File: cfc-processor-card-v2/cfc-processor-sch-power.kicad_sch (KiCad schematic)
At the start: 93 parts, among them Q2 PMV45EN, Q3 DMP2240UDM, Q4 PMV45EN, Q5 DMP3050LVT-7, Q6 DMP3050LVT-7, U12 MIC842LYC5, U13 MIC842LYC5, U14 MAX4211FETE, U15 TPS62112, U16 MAX7310ATE+, U5 TS5A21366

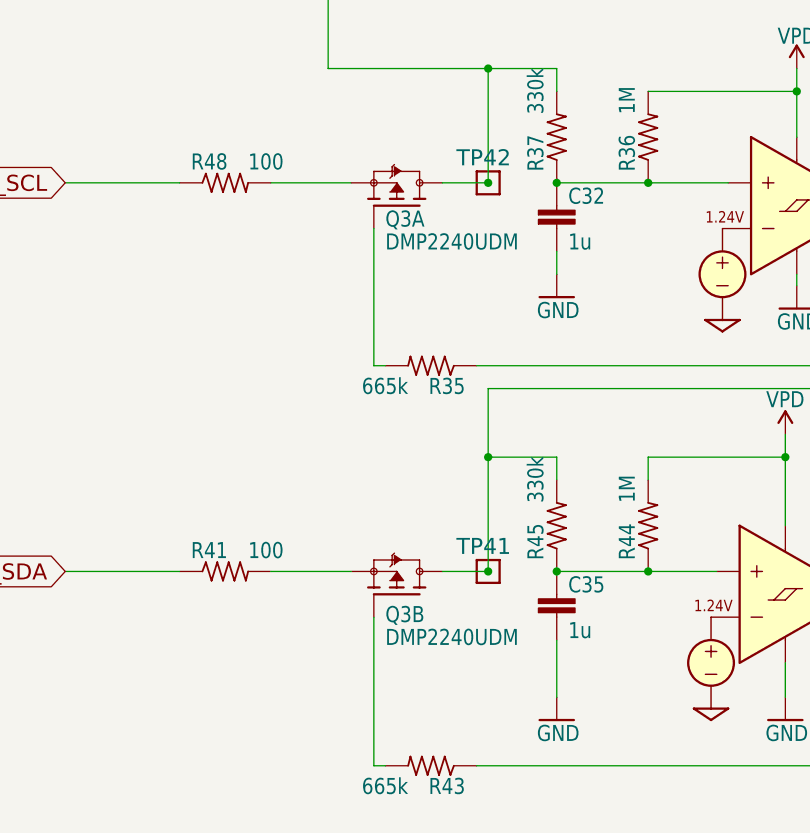
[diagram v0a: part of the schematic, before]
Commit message: Fixed up crappy symbol on OPD; no change to layout, just schematic and link to PCB.
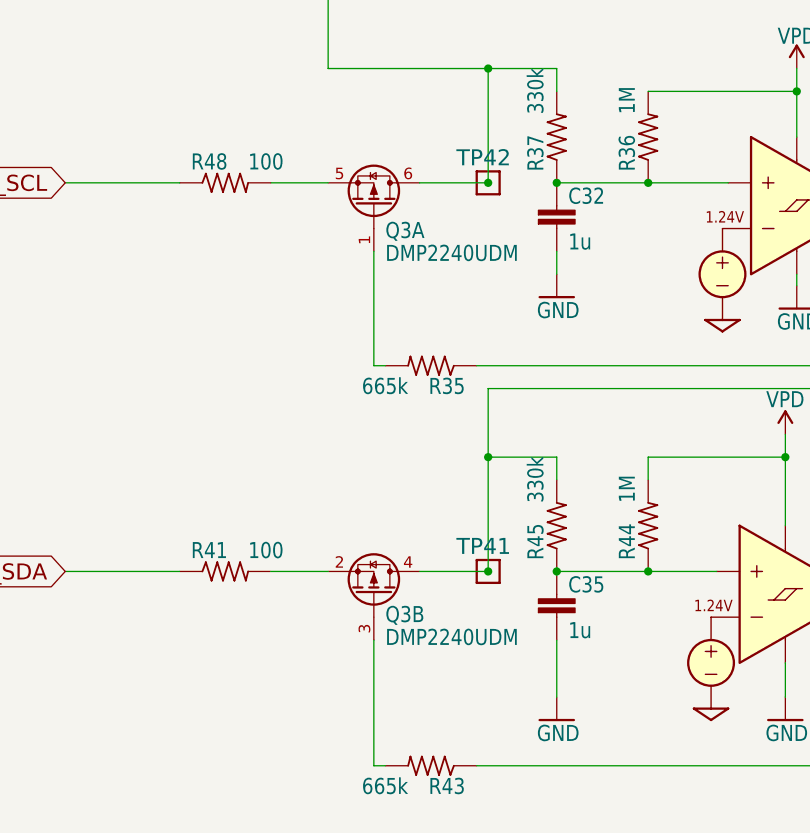
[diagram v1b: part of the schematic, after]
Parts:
- Q3: symbol cfc-card-eagle-import:Q-MOSFET-PCH-dual-SOT23-6_MOSFET-PCH-SOT23-6 -> Transistor_FET:Q_Dual_PMOS_G1S2G2D2S1D1
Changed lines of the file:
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@@
 	(wire
 		(pts
-			(xy 92.71 245.11) (xy 92.71 228.6)
+			(xy 92.71 245.11) (xy 92.71 231.14)
 		)
 		(stroke
@@
 	(wire
 		(pts
-			(xy 105.41 180.34) (xy 100.33 180.34)
+			(xy 105.41 180.34) (xy 97.79 180.34)
 		)
 		(stroke
@@
 	(wire
 		(pts
-			(xy 90.17 223.52) (xy 81.28 223.52)
+			(xy 87.63 223.52) (xy 81.28 223.52)
 		)
 		(stroke
@@
 	(wire
 		(pts
-			(xy 92.71 200.66) (xy 92.71 185.42)
+			(xy 92.71 200.66) (xy 92.71 187.96)
 		)
 		(stroke
@@
 	(wire
 		(pts
-			(xy 105.41 223.52) (xy 100.33 223.52)
+			(xy 105.41 223.52) (xy 97.79 223.52)
 		)
 		(stroke
@@
 	(wire
 		(pts
-			(xy 90.17 180.34) (xy 81.28 180.34)
+			(xy 87.63 180.34) (xy 81.28 180.34)
 		)
 		(stroke
@@
 	)
 	(symbol
-		(lib_id "cfc-card-eagle-import:Q-MOSFET-PCH-dual-SOT23-6_MOSFET-PCH-SOT23-6")
-		(at 95.25 226.06 90)
+		(lib_id "Transistor_FET:Q_Dual_PMOS_G1S2G2D2S1D1")
+		(at 92.71 226.06 270)
+		(mirror x)
 		(unit 2)
 		(exclude_from_sim no)
@@
 					(size 1.778 1.5113)
 				)
-				(justify right top)
+				(justify left top)
 			)
 		)
@@
 					(size 1.778 1.5113)
 				)
-				(justify right top)
+				(justify left top)
 			)
 		)
 		(property "Footprint" "Package_TO_SOT_SMD:SOT-23-6"
-			(at 95.25 226.06 0)
+			(at 92.71 224.79 0)
 			(effects
 				(font
@@
 			)
 		)
-		(property "Datasheet" "https://www.diodes.com/assets/Datasheets/ds31197.pdf"
-			(at 95.25 226.06 0)
+		(property "Datasheet" "~"
+			(at 92.71 224.79 0)
 			(effects
 				(font
@@
 			)
 		)
-		(property "Description" "Dual Mosfet Array 20V 2A 600mW Surface Mount SOT-26"
-			(at 95.25 226.06 0)
+		(property "Description" "Dual PMOS transistor, 6 pin package"
+			(at 92.71 226.06 0)
 			(effects
 				(font
@@
 		)
 		(property "DIS" "DigiKey"
-			(at 95.25 226.06 90)
+			(at 92.71 226.06 90)
 			(effects
 				(font
@@
 		)
 		(property "DPN" "DMP2240UDMDICT-ND"
-			(at 95.25 226.06 90)
+			(at 92.71 226.06 90)
 			(effects
 				(font
@@
 		)
 		(property "MFR" "Diodes Inc"
-			(at 95.25 226.06 90)
+			(at 92.71 226.06 90)
 			(effects
 				(font
@@
 		)
 		(property "MPN" "DMP2240UDM"
-			(at 95.25 226.06 90)
+			(at 92.71 226.06 90)
 			(effects
 				(font
@@
 			)
 		)
+		(property "Value_1" ""
+			(at 92.71 226.06 0)
+			(effects
+				(font
+					(size 1.778 1.5113)
+				)
+				(justify left bottom)
+				(hide yes)
+			)
+		)
 		(pin "1"
 		)
@@
 	)
 	(symbol
-		(lib_id "cfc-card-eagle-import:Q-MOSFET-PCH-dual-SOT23-6_MOSFET-PCH-SOT23-6")
-		(at 95.25 182.88 90)
+		(lib_id "Transistor_FET:Q_Dual_PMOS_G1S2G2D2S1D1")
+		(at 92.71 182.88 270)
+		(mirror x)
 		(unit 1)
 		(exclude_from_sim no)
@@
 		(dnp no)
 		(property "Reference" "Q3"
-			(at 93.98 185.42 90)
+			(at 93.98 186.69 90)
 			(effects
 				(font
 					(size 1.778 1.5113)
 				)
-				(justify right top)
+				(justify left top)
 			)
 		)
 		(property "Value" "DMP2240UDM"
-			(at 93.98 187.96 90)
+			(at 93.98 189.23 90)
 			(effects
 				(font
 					(size 1.778 1.5113)
 				)
-				(justify right top)
+				(justify left top)
 			)
 		)
 		(property "Footprint" "Package_TO_SOT_SMD:SOT-23-6"
-			(at 95.25 182.88 0)
+			(at 92.71 181.61 0)
 			(effects
 				(font
@@
 			)
 		)
-		(property "Datasheet" "https://www.diodes.com/assets/Datasheets/ds31197.pdf"
-			(at 95.25 182.88 0)
+		(property "Datasheet" "~"
+			(at 92.71 181.61 0)
 			(effects
 				(font
@@
 			)
 		)
-		(property "Description" "Dual Mosfet Array 20V 2A 600mW Surface Mount SOT-26"
-			(at 95.25 182.88 0)
+		(property "Description" "Dual PMOS transistor, 6 pin package"
+			(at 92.71 182.88 0)
 			(effects
 				(font
@@
 		)
 		(property "DIS" "DigiKey"
-			(at 95.25 182.88 90)
+			(at 92.71 182.88 90)
 			(effects
 				(font
@@
 		)
 		(property "DPN" "DMP2240UDMDICT-ND"
-			(at 95.25 182.88 90)
+			(at 92.71 182.88 90)
 			(effects
 				(font
@@
 		)
 		(property "MFR" "Diodes Inc"
-			(at 95.25 182.88 90)
+			(at 92.71 182.88 90)
 			(effects
 				(font
@@
 		)
 		(property "MPN" "DMP2240UDM"
-			(at 95.25 182.88 90)
+			(at 92.71 182.88 90)
 			(effects
 				(font
@@
 				(hide yes)
 			)
+		)
+		(property "Value_1" ""
+			(at 92.71 182.88 0)
+			(effects
+				(font
+					(size 1.778 1.5113)
+				)
+				(justify left bottom)
+				(hide yes)
+			)

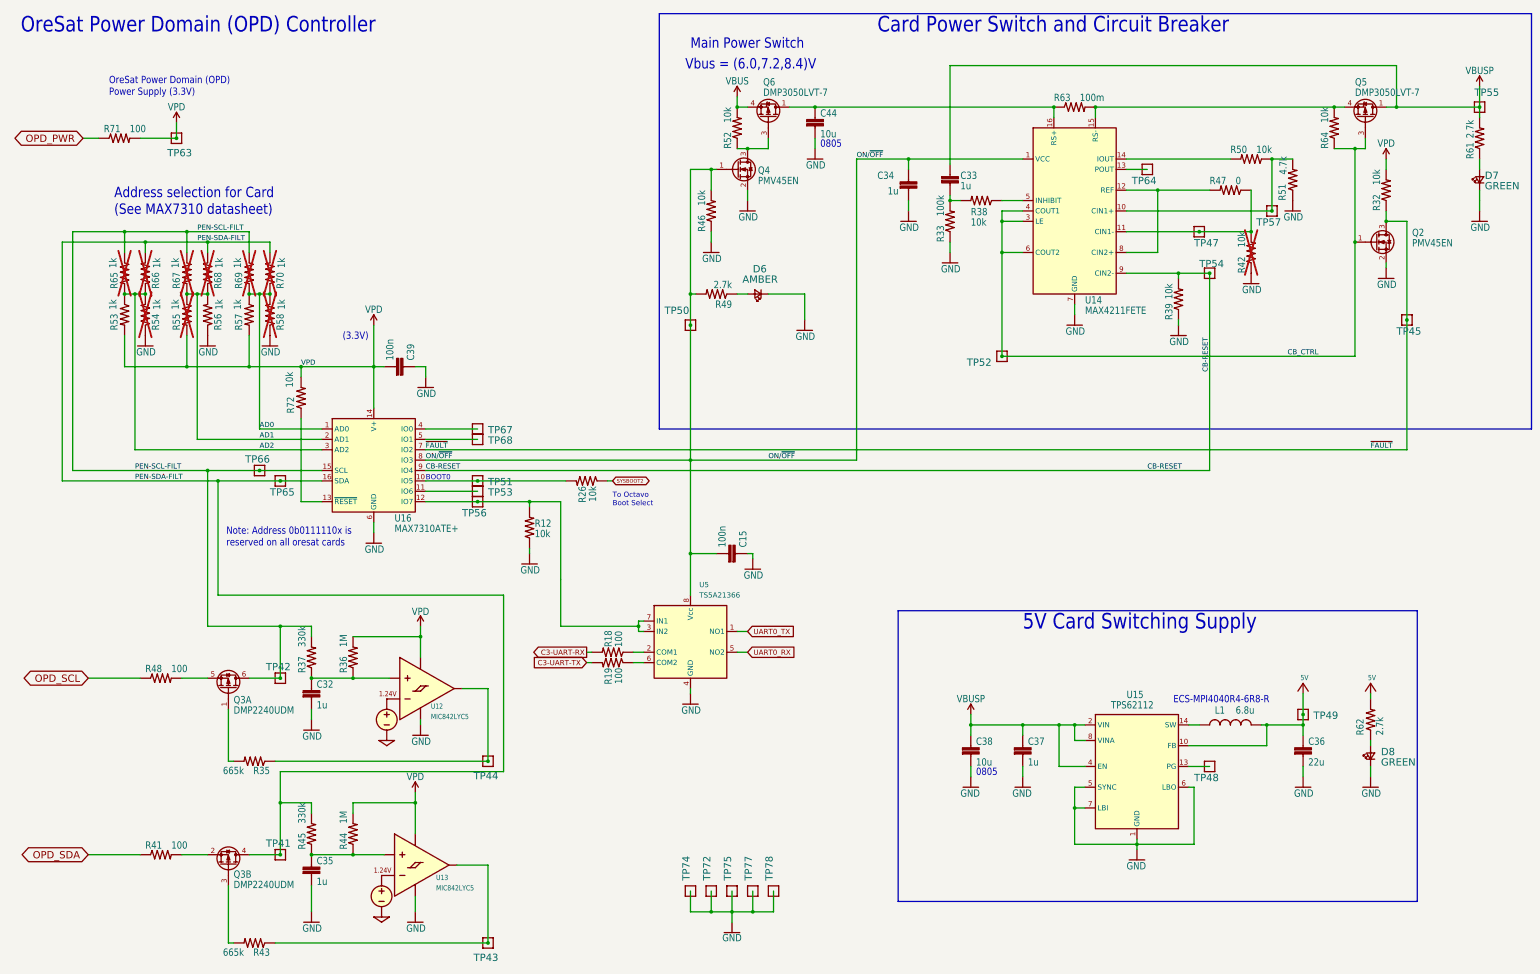
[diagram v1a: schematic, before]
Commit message: CFC processor schematic Change
changed to hierarchy view, changed all global net labels to hierarchy labels, changed all resistor, capacitor, and ground symbols to modern oresat labels. Deleted connectors sheet and added .history to gitignore.
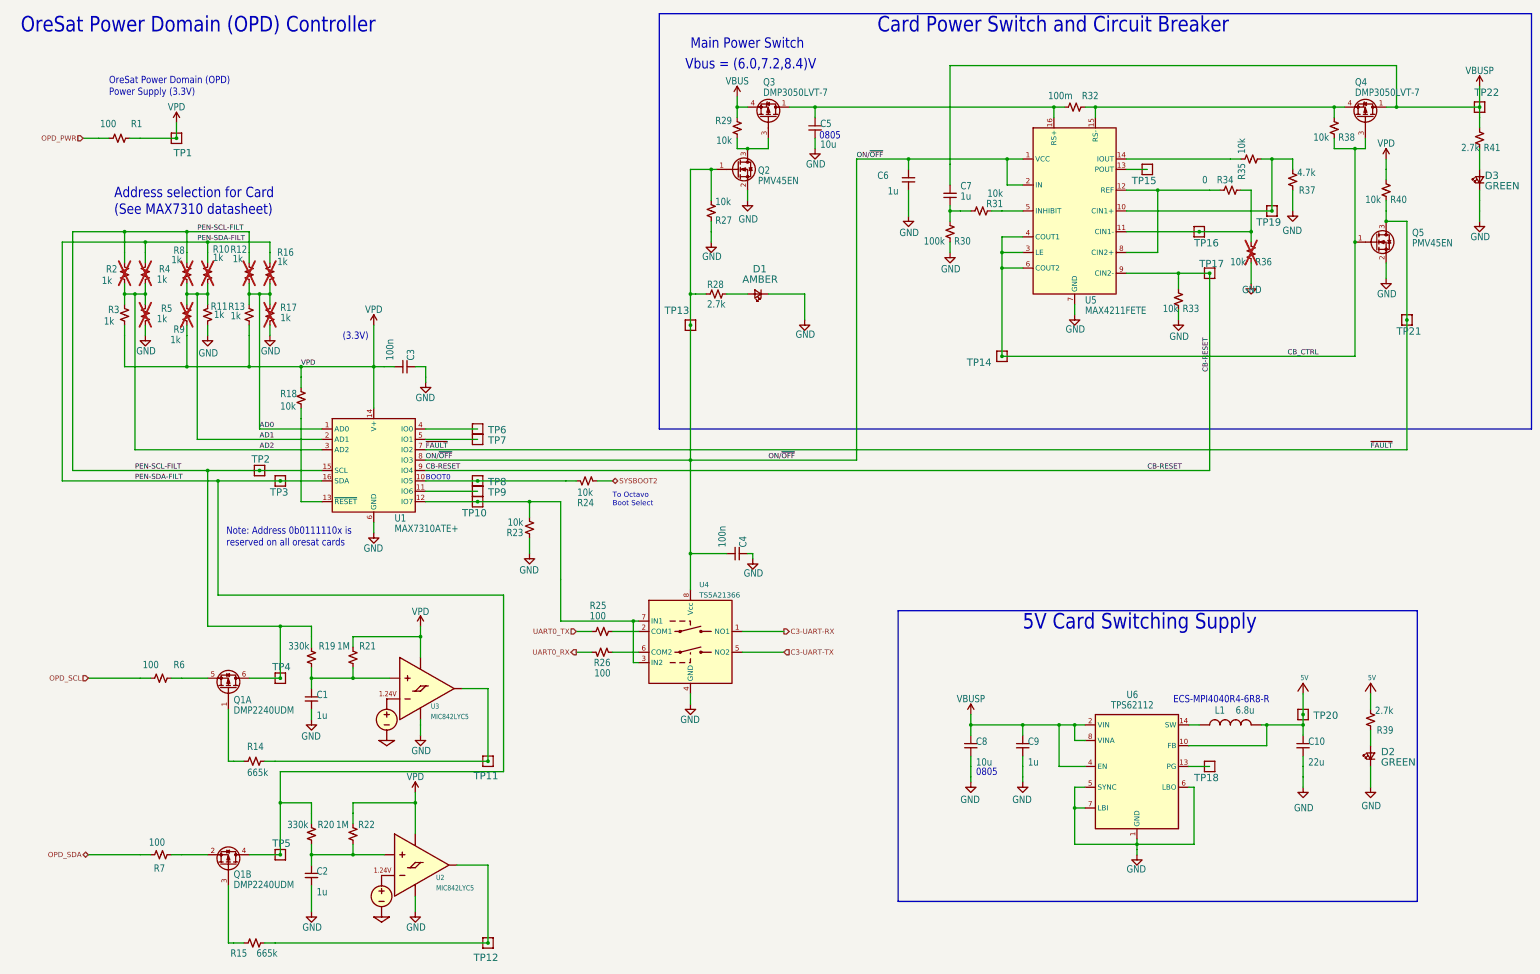
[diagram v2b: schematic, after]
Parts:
- removed TP72, TP74, TP75, TP77, TP78: TEST-POINT, cfc-card:2MM-TEST-POINT, symbol cfc-card-eagle-import:TEST-POINT
- C1: renamed from C32; symbol cfc-card-eagle-import:C-EU0805-B-NOSILK -> Device:C_Small
- C10: renamed from C36; symbol cfc-card-eagle-import:C-EUC1210 -> Device:C_Small
- C2: renamed from C35; symbol cfc-card-eagle-import:C-EU0805-B-NOSILK -> Device:C_Small
- C3: renamed from C39; symbol cfc-card-eagle-import:C-EU0603-A -> Device:C_Small
- C4: renamed from C15; symbol cfc-card-eagle-import:C-EU0603-A -> Device:C_Small
- C5: renamed from C44; symbol cfc-card-eagle-import:C-EU0805-B -> Device:C_Small
- C6: renamed from C34; symbol cfc-card-eagle-import:C-EU0603-A -> Device:C_Small
- C7: renamed from C33; symbol cfc-card-eagle-import:C-EU0603-A -> Device:C_Small
- C8: renamed from C38; symbol cfc-card-eagle-import:C-EU0805-B -> Device:C_Small
- C9: renamed from C37; symbol cfc-card-eagle-import:C-EU0603-A -> Device:C_Small
- R1: renamed from R71; symbol cfc-card-eagle-import:R-US_0603-A -> Device:R_Small_US
- R10: renamed from R68; symbol cfc-card-eagle-import:R-US_0603-A -> Device:R_Small_US
- R11: renamed from R56; symbol cfc-card-eagle-import:R-US_0603-A -> Device:R_Small_US
- R12: renamed from R69; symbol cfc-card-eagle-import:R-US_0603-A -> Device:R_Small_US
- R13: renamed from R57; symbol cfc-card-eagle-import:R-US_0603-A -> Device:R_Small_US
- R14: renamed from R35; symbol cfc-card-eagle-import:R-US_0603-A -> Device:R_Small_US
- R15: renamed from R43; symbol cfc-card-eagle-import:R-US_0603-A -> Device:R_Small_US
- R16: renamed from R70; symbol cfc-card-eagle-import:R-US_0603-A -> Device:R_Small_US
- R17: renamed from R58; symbol cfc-card-eagle-import:R-US_0603-A -> Device:R_Small_US
- R18: renamed from R72; symbol cfc-card-eagle-import:R-US_0603-A -> Device:R_Small_US
- R19: renamed from R37; symbol cfc-card-eagle-import:R-US_0603-A -> Device:R_Small_US
- R2: renamed from R65; symbol cfc-card-eagle-import:R-US_0603-A -> Device:R_Small_US
- R20: renamed from R45; symbol cfc-card-eagle-import:R-US_0603-A -> Device:R_Small_US
- R21: renamed from R36; symbol cfc-card-eagle-import:R-US_0603-A -> Device:R_Small_US
- R22: renamed from R44; symbol cfc-card-eagle-import:R-US_0603-A -> Device:R_Small_US
- R23: renamed from R12; symbol cfc-card-eagle-import:R-US_0603-A -> Device:R_Small_US
- R24: renamed from R26; symbol cfc-card-eagle-import:R-US_0603-A -> Device:R_Small_US
- R25: renamed from R18; symbol cfc-card-eagle-import:R-US_0603-A -> Device:R_Small_US
- R26: renamed from R19; symbol cfc-card-eagle-import:R-US_0603-A -> Device:R_Small_US
- R27: renamed from R46; symbol cfc-card-eagle-import:R-US_0603-A -> Device:R_Small_US
- R28: renamed from R49; symbol cfc-card-eagle-import:R-US_0603-A -> Device:R_Small_US
- R29: renamed from R52; symbol cfc-card-eagle-import:R-US_0603-A -> Device:R_Small_US
- R3: renamed from R53; symbol cfc-card-eagle-import:R-US_0603-A -> Device:R_Small_US
- R30: renamed from R33; symbol cfc-card-eagle-import:R-US_0603-A -> Device:R_Small_US
- R31: renamed from R38; symbol cfc-card-eagle-import:R-US_0603-A -> Device:R_Small_US
- R32: renamed from R63; symbol cfc-card-eagle-import:rcl_334_R-US_R1206 -> Device:R_Small_US
- R33: renamed from R39; symbol cfc-card-eagle-import:R-US_0603-A -> Device:R_Small_US
- R34: renamed from R47; symbol cfc-card-eagle-import:R-US_0603-A -> Device:R_Small_US
- R35: renamed from R50; symbol cfc-card-eagle-import:R-US_0603-A -> Device:R_Small_US
- R36: renamed from R42; symbol cfc-card-eagle-import:R-US_0603-A -> Device:R_Small_US
- R37: renamed from R51; symbol cfc-card-eagle-import:R-US_0603-A -> Device:R_Small_US
- R38: renamed from R64; symbol cfc-card-eagle-import:R-US_0603-A -> Device:R_Small_US
- R39: renamed from R62; symbol cfc-card-eagle-import:R-US_0603-A -> Device:R_Small_US
- R4: renamed from R66; symbol cfc-card-eagle-import:R-US_0603-A -> Device:R_Small_US
- R40: renamed from R32; symbol cfc-card-eagle-import:R-US_0603-A -> Device:R_Small_US
- R41: renamed from R61; symbol cfc-card-eagle-import:R-US_0603-A -> Device:R_Small_US
- R5: renamed from R54; symbol cfc-card-eagle-import:R-US_0603-A -> Device:R_Small_US
- R6: renamed from R48; symbol cfc-card-eagle-import:R-US_0603-A -> Device:R_Small_US
- R7: renamed from R41; symbol cfc-card-eagle-import:R-US_0603-A -> Device:R_Small_US
- R8: renamed from R67; symbol cfc-card-eagle-import:R-US_0603-A -> Device:R_Small_US
- R9: renamed from R55; symbol cfc-card-eagle-import:R-US_0603-A -> Device:R_Small_US
- U4: renamed from U5; MFR Texas Instruments -> Texas Instruments
- U5: renamed from U14; symbol oresat-ics:MAX4211FETE -> oresat-ics:MAX4211D/E/F
- renumbered D6 to D1, D8 to D2, D7 to D3, Q3 to Q1, Q4 to Q2, Q6 to Q3, Q5 to Q4, Q2 to Q5, TP63 to TP1, TP56 to TP10, TP44 to TP11, TP43 to TP12, TP50 to TP13, TP52 to TP14, TP64 to TP15, TP47 to TP16, TP54 to TP17, TP48 to TP18, TP57 to TP19, TP66 to TP2, TP49 to TP20, TP45 to TP21, TP55 to TP22, TP65 to TP3, TP42 to TP4, TP41 to TP5, TP67 to TP6, TP68 to TP7, TP51 to TP8, TP53 to TP9, U16 to U1, U13 to U2, U12 to U3, U15 to U6
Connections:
- net AD0: now also R16.2, R17.1; no longer R16.1, R17.2
- net AD1: now also R10.2, R11.1; no longer R10.1, R11.2
- net AD2: now also R4.2, R5.1; no longer R4.1, R5.2
- net C3-UART-RX: now also U4.1 (NO1); no longer R25.2
- net C3-UART-TX: now also U4.5 (NO2); no longer R26.2
- net GND: now also R11.2, R17.2, R5.2; no longer R11.1, R17.1, R5.1
- net ON/~{OFF}: now also U5.2 (IN)
- net PEN-SDA-FILT: now also R10.1, R16.1, R4.1; no longer R10.2, R16.2, R4.2
- net SYSBOOT2: now also R24.2; no longer R24.1
- net UART0_RX: now also R26.1; no longer U4.5 (NO2)
- net UART0_TX: now also R25.2; no longer U4.1 (NO1)
- net at U4.6 (COM2): now also R26.2; no longer R26.1
- net at TP8.1, U1.10 (IO5): now also R24.1; no longer R24.2
